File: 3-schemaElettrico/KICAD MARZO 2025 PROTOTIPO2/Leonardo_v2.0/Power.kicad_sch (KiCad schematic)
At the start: 3 parts

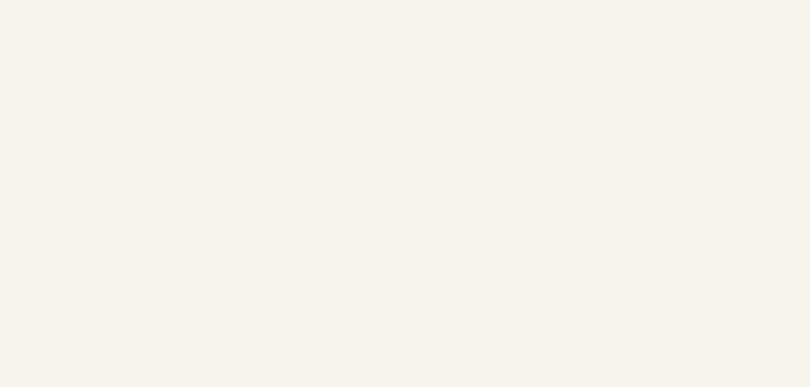
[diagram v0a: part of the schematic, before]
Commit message: done 74hc238
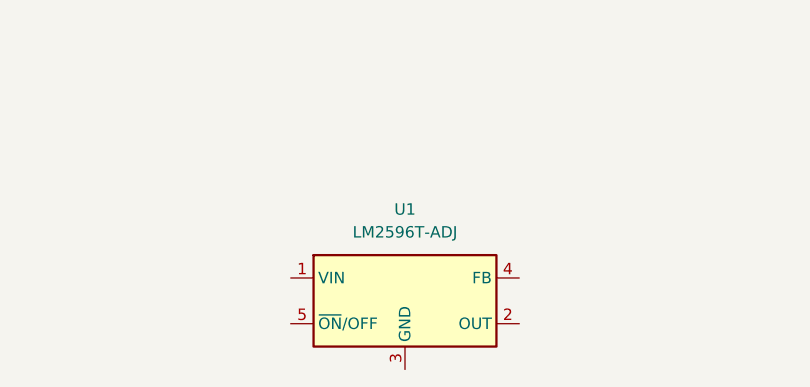
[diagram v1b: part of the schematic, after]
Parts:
- added U1: LM2596T-ADJ, Package_TO_SOT_THT:TO-220-5_P3.4x3.7mm_StaggerOdd_Lead3.8mm_Vertical, symbol Regulator_Switching:LM2596T-ADJ
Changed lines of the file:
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@@
+	)
+	(symbol
+		(lib_id "Regulator_Switching:LM2596T-ADJ")
+		(at 170.18 96.52 0)
+		(unit 1)
+		(exclude_from_sim no)
+		(in_bom yes)
+		(on_board yes)
+		(dnp no)
+		(fields_autoplaced yes)
+		(property "Reference" "U1"
+			(at 170.18 86.36 0)
+			(effects
+				(font
+					(size 1.27 1.27)
+				)
+			)
+		)
+		(property "Value" "LM2596T-ADJ"
+			(at 170.18 88.9 0)
+			(effects
+				(font
+					(size 1.27 1.27)
+				)
+			)
+		)
+		(property "Footprint" "Package_TO_SOT_THT:TO-220-5_P3.4x3.7mm_StaggerOdd_Lead3.8mm_Vertical"
+			(at 171.45 102.87 0)
+			(effects
+				(font
+					(size 1.27 1.27)
+					(italic yes)
+				)
+				(justify left)
+				(hide yes)
+			)
+		)
+		(property "Datasheet" "http://www.ti.com/lit/ds/symlink/lm2596.pdf"
+			(at 170.18 96.52 0)
+			(effects
+				(font
+					(size 1.27 1.27)
+				)
+				(hide yes)
+			)
+		)
+		(property "Description" "Adjustable 3A 150kHz Step-Down Voltage Regulator, TO-220"
+			(at 170.18 96.52 0)
+			(effects
+				(font
+					(size 1.27 1.27)
+				)
+				(hide yes)
+			)
+		)
+		(pin "5"
+		)
+		(pin "3"
+		)
+		(pin "4"
+		)
+		(pin "2"
+		)
+		(pin "1"
+		)
+		(instances
+			(project ""
+				(path "/0d3207ba-e51c-4f46-8c4e-e116d0062888/bece2dc1-1740-4c5c-8fd4-4c4b8478fa00"
+					(reference "U1")
+					(unit 1)
+				)
+			)
+		)
 	)
 	(symbol
